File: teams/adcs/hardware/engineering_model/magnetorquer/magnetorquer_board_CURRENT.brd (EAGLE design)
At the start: 90 x 90 mm, 40 parts

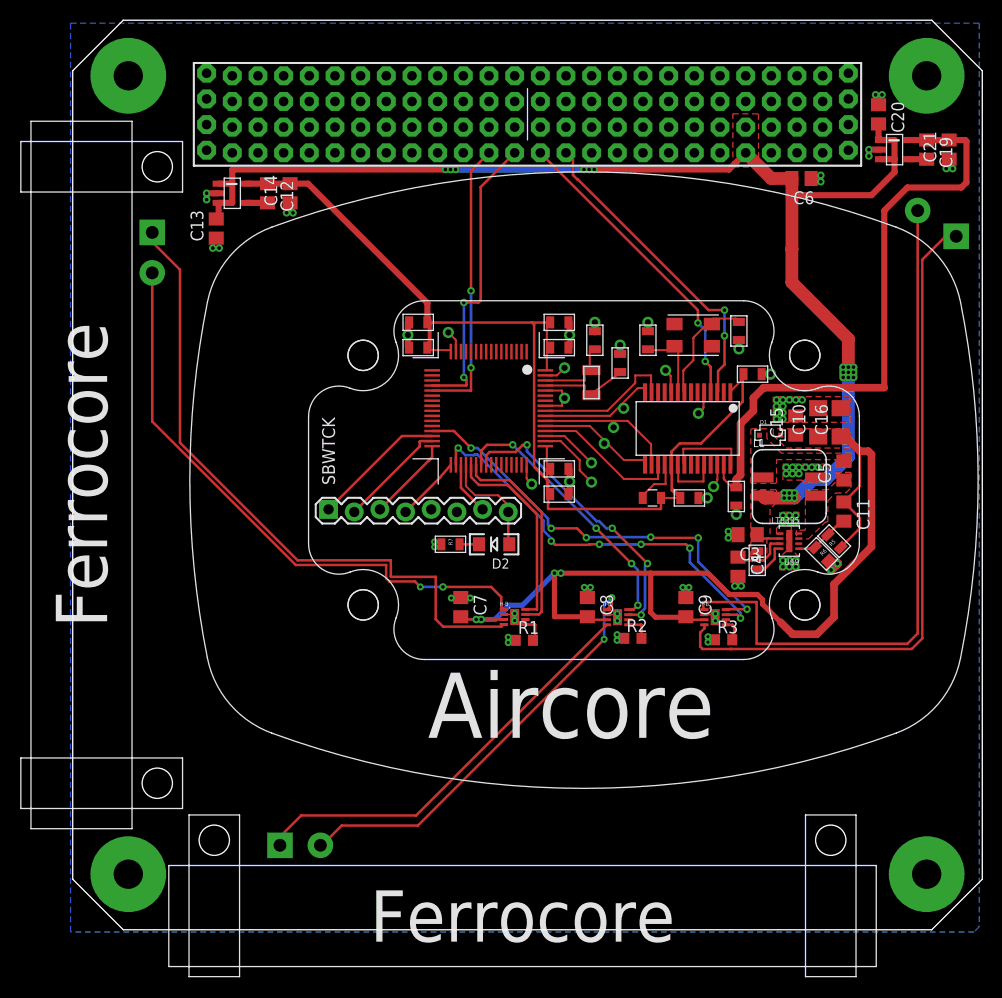
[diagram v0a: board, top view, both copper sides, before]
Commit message: ADCS/MT: Relabel component values and tidy up schematic
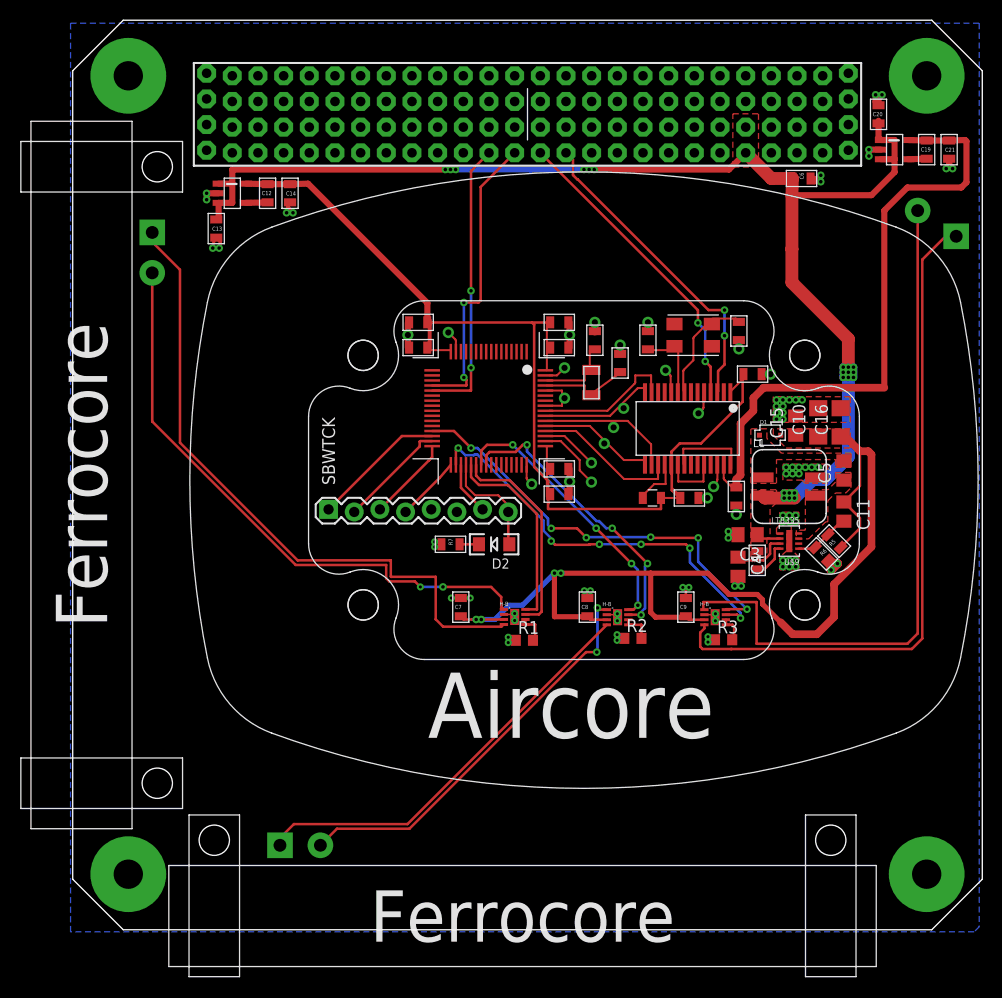
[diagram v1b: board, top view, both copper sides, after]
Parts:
- C12, C13, C14, C19, C20, C21, C6, C7, C8, C9: device rcl:C0805 -> DubSat1 Components:0805
- R7: value (none) -> 330
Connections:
- net 6V renamed V_TORQ
- net N$10 renamed MT_X_B
- net N$11 renamed MT_X_A
- net N$12 renamed MT_Y_A
- net N$13 renamed MT_Y_B
- net N$14 renamed MT_Z_B
- net N$15 renamed MT_Z_A
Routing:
- net MT_Y_B: track 44.4 -> 40.7 mm
- net V_TORQ: track 100.0 -> 97.6 mm
- net GND: track 39.9 -> 38.2 mm
